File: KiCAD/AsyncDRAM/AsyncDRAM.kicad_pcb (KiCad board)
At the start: 2 copper layers, 13 parts, among them J1 UART, J2 SPI, J3 UPDI, J4 POWER

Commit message: Adjusted Design Rules, added MT6205 BGA footprint for fun
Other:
- net class Default: clearance 0.2 -> 0.2032; trace_width 0.25 -> 0.2032; via_dia 0.8 -> 0.9
- rule trace_clearance: 0.2 -> 0.2032
- rule trace_min: 0.2 -> 0.089
- rule via_min_drill: 0.3 -> 0.2
- rule via_min_size: 0.4 -> 0.45
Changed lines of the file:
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@@
   )
   (setup
-    (last_trace_width 0.25)
-    (trace_clearance 0.2)
+    (last_trace_width 0.2032)
+    (user_trace_width 0.089)
+    (trace_clearance 0.2032)
     (zone_clearance 0.508)
     (zone_45_only no)
-    (trace_min 0.2)
-    (via_size 0.8)
+    (trace_min 0.089)
+    (via_size 0.9)
     (via_drill 0.4)
-    (via_min_size 0.4)
-    (via_min_drill 0.3)
+    (via_min_size 0.45)
+    (via_min_drill 0.2)
+    (user_via 0.45 0.2)
     (uvia_size 0.3)
     (uvia_drill 0.1)
@@
   (net 40 MOSI)
   (net_class Default "This is the default net class."
-    (clearance 0.2)
-    (trace_width 0.25)
-    (via_dia 0.8)
+    (clearance 0.2032)
+    (trace_width 0.2032)
+    (via_dia 0.9)
     (via_drill 0.4)
     (uvia_dia 0.3)

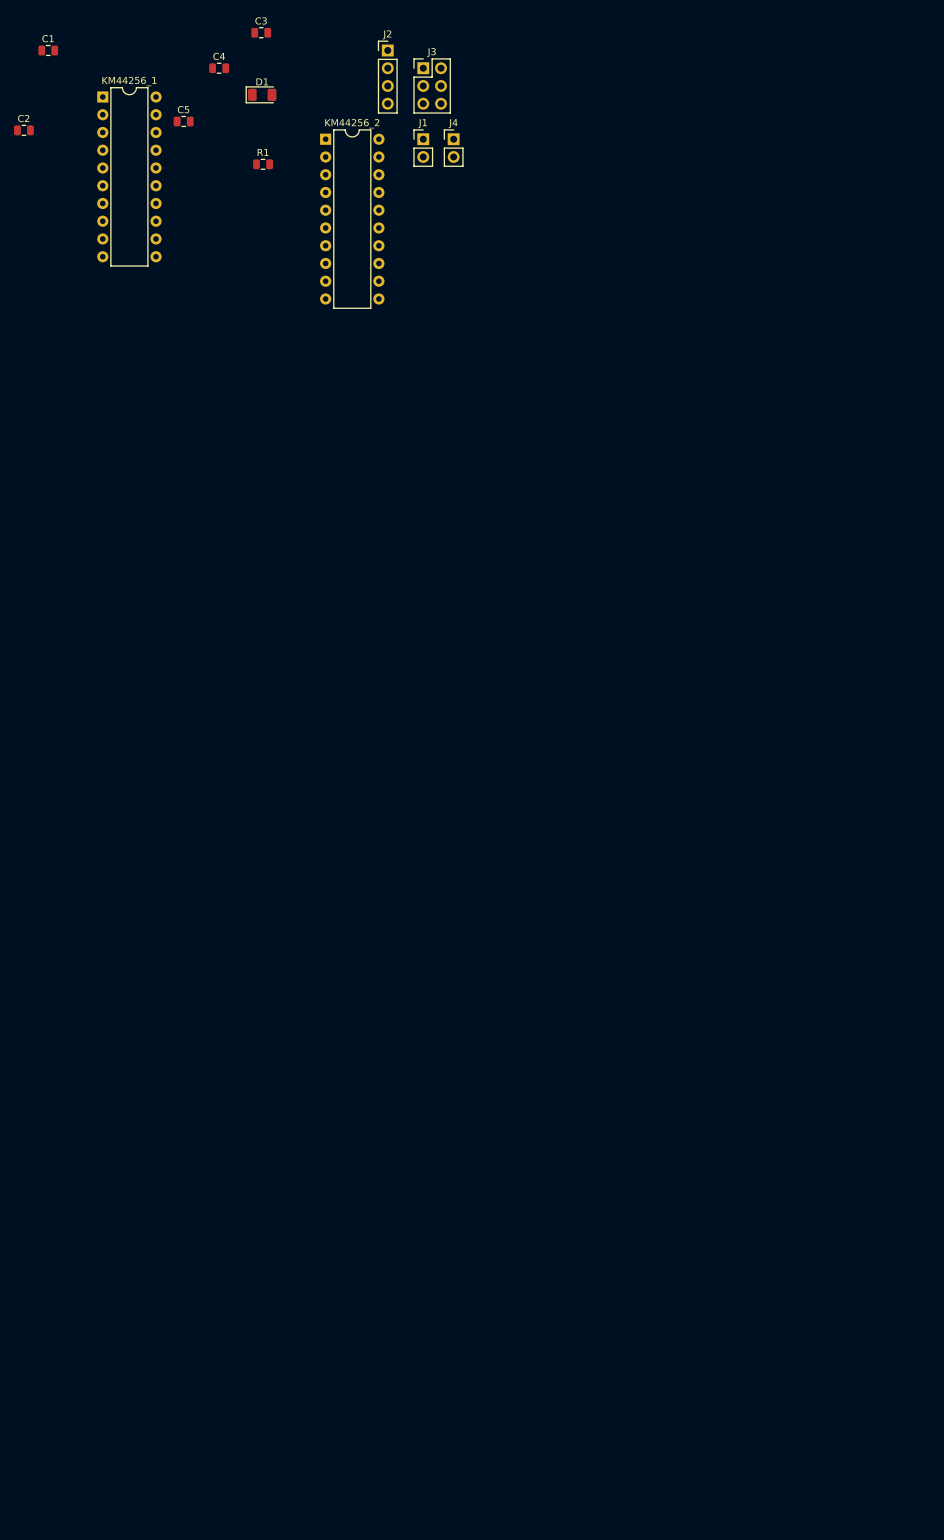
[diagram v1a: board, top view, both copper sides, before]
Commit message: Finalizing schematic, adding TQFP footprint, PCB outline
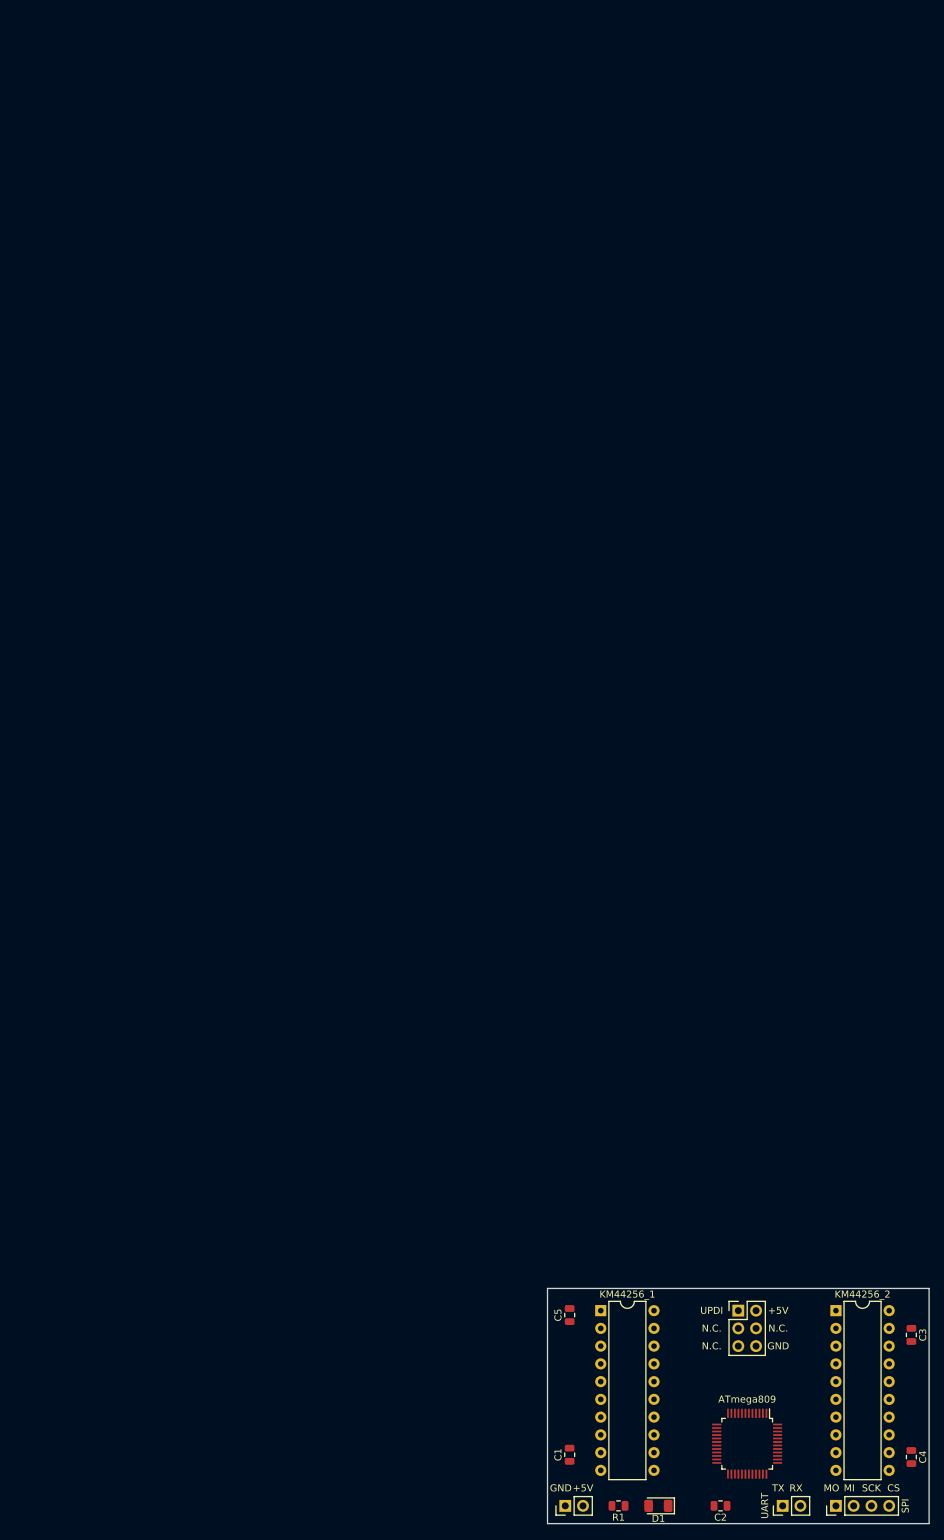
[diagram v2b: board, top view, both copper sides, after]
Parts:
- added ATmega809: ATmega809, QFP:TQFP-48_7x7mm_P0.5mm, F.Cu at (43.8, 184.2)
- moved C4 222.1 mm to (67.3, 186.1), turned to 270 degrees
- moved C2 220.7 mm to (40.0, 193.0), turned to 180 degrees
- moved J2 217.9 mm to (56.5, 193.0), turned to 90 degrees
- moved C1 214.4 mm to (18.4, 185.7), turned to 90 degrees
- moved D1 209.7 mm to (31.1, 193.0), turned to 180 degrees
- moved C3 208.3 mm to (67.3, 168.6), turned to 270 degrees
- moved J1 202.2 mm to (48.9, 193.0), turned to 90 degrees
- moved R1 198.6 mm to (25.4, 193.0), turned to 180 degrees
- moved J4 196.2 mm to (17.8, 193.0), turned to 90 degrees
- moved KM44256_1 187.7 mm to (22.9, 165.1)
- moved J3 183.4 mm to (42.5, 165.1)
- moved KM44256_2 182.9 mm to (56.5, 165.1)
- moved C5 179.5 mm to (18.4, 165.7), turned to 90 degrees
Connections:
- net Net-(ATM809_1-Pad1) renamed A0
- net Net-(ATM809_1-Pad2) renamed A1
- net Net-(ATM809_1-Pad3) renamed A2
- net Net-(ATM809_1-Pad4) renamed A3
- net Net-(ATM809_1-Pad5) renamed A4
- net Net-(ATM809_1-Pad6) renamed A5
- net Net-(ATM809_1-Pad7) renamed A6
- net Net-(ATM809_1-Pad8) renamed A7
- net Net-(ATM809_1-Pad9) renamed A8
- KM44256_1 pad 16: Net-(KM44256_1-Pad16) -> ~OE
- KM44256_1 pad 17: Net-(KM44256_1-Pad17) -> ~CAS
- KM44256_1 pad 3: Net-(KM44256_1-Pad3) -> ~W
- KM44256_1 pad 4: Net-(KM44256_1-Pad4) -> ~RAS
- KM44256_2 pad 16: Net-(KM44256_2-Pad16) -> ~OE
- KM44256_2 pad 17: Net-(KM44256_2-Pad17) -> ~CAS
- KM44256_2 pad 3: Net-(KM44256_2-Pad3) -> ~W
- KM44256_2 pad 4: Net-(KM44256_2-Pad4) -> ~RAS
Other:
- board outline added: 54.6 x 33.7 mm
- board text added: "+5V"
- board text added: "CS"
- board text added: "GND"
- board text added: "MI"
- board text added: "MO"
- board text added: "N.C."
- board text added: "RX"
- board text added: "SCK"
- board text added: "TX"
- board text added: "UPDI"

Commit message: GND Planes
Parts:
- turned ATmega809 to 0 degrees
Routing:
- added copper zone on B.Cu, net GND
- added copper zone on F.Cu, net GND
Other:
- net class Default: clearance 0.2032 -> 0.127
- rule trace_clearance: 0.2032 -> 0.127
- board text removed: "N.C."

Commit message: Adjusted board settings to Elecrow Specifications
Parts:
- renumbered ATmega809 to ATM809_1
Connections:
- net Net-(ATM809_1-Pad41) renamed UPDI
- D1 pad 1: GND -> Net-(D1-Pad1)
- D1 pad 2: Net-(D1-Pad2) -> +5V
- R1 pad 1: Net-(D1-Pad2) -> GND
- R1 pad 2: +5V -> Net-(D1-Pad1)
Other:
- net class Default: clearance 0.127 -> 0.1524; trace_width 0.2032 -> 0.1524; via_dia 0.9 -> 0.6048; via_drill 0.4 -> 0.3
- rule trace_clearance: 0.127 -> 0.1524
- rule trace_min: 0.089 -> 0.1524
- rule via_min_drill: 0.2 -> 0.3
- rule via_min_size: 0.45 -> 0.6048

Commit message: Started PCB Routing...
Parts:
- turned ATM809_1 to 90 degrees
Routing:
- net +5V: track 0.00 -> 83.4 mm
- net A0: track 0.00 -> 53.9 mm, vias 0 -> 1
- net A3: track 0.00 -> 53.2 mm, vias 0 -> 3
- net A7: track 0.00 -> 51.6 mm, vias 0 -> 2
- net A6: track 0.00 -> 48.9 mm, vias 0 -> 2
- net A4: track 0.00 -> 45.5 mm
- net A5: track 0.00 -> 45.3 mm, vias 0 -> 2
- net A1: track 0.00 -> 33.6 mm, vias 0 -> 1
- net A2: track 0.00 -> 32.0 mm
- net Net-(D1-Pad1): track 0.00 -> 9.53 mm
- net A8: track 0.00 -> 2.74 mm

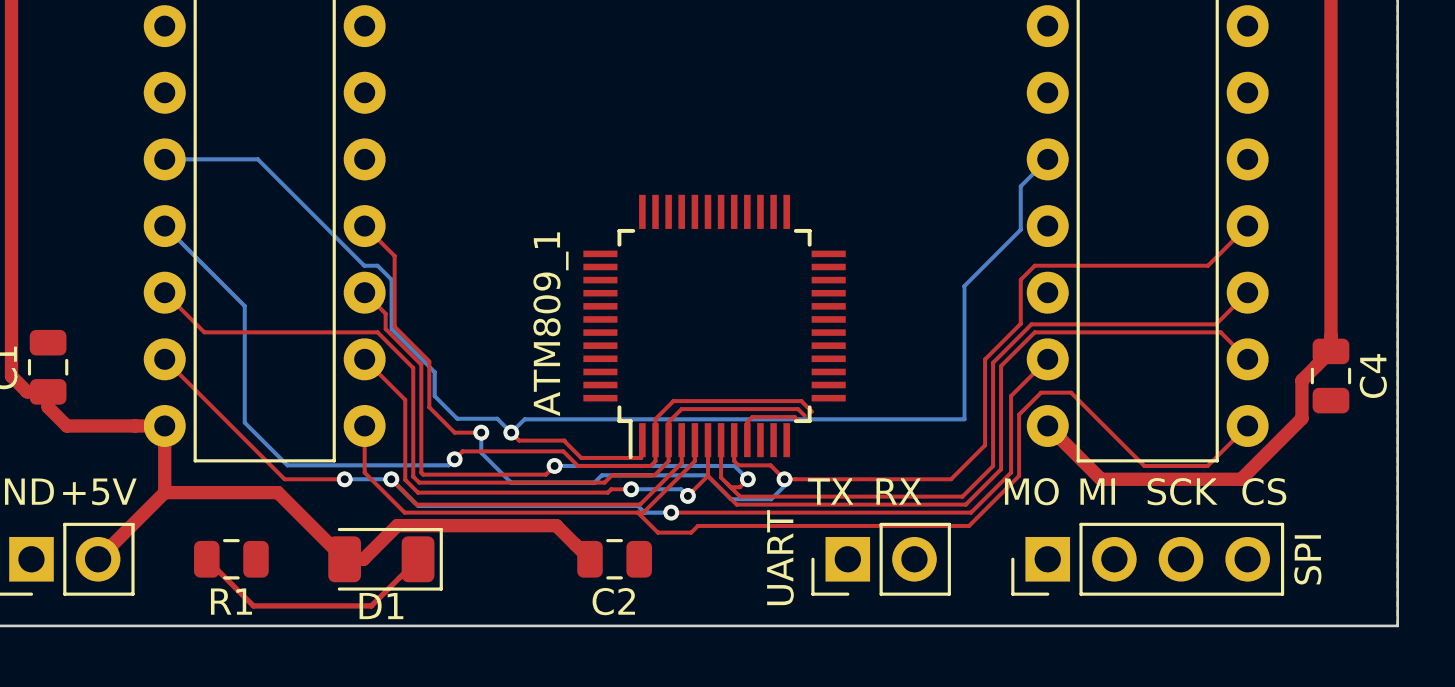
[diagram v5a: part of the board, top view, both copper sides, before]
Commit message: PCB Routing Update
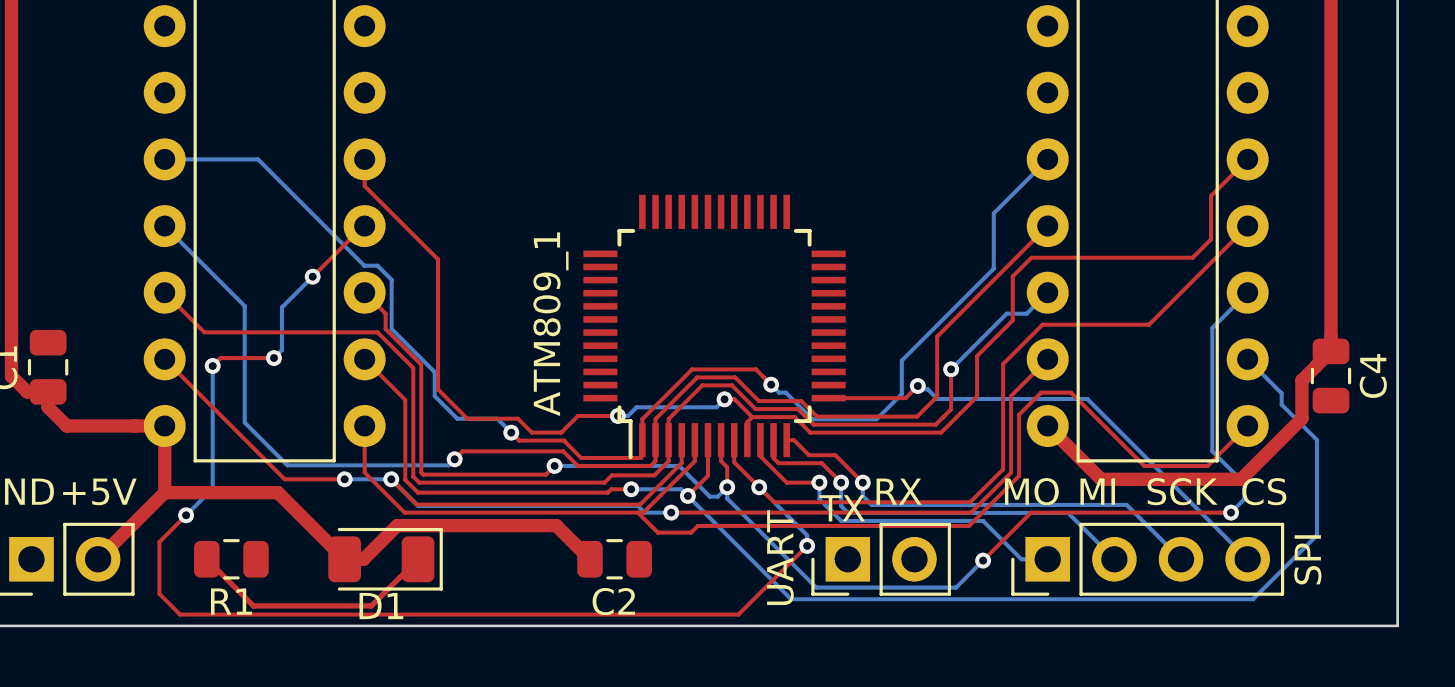
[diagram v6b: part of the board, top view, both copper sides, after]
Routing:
- net A8: track 2.74 -> 50.6 mm, vias 0 -> 2
- net A7: track 51.6 -> 75.3 mm, vias 2 -> 6
- net SS: track 0.00 -> 18.9 mm, vias 0 -> 1
- net SCK: track 0.00 -> 17.2 mm, vias 0 -> 1
- net MISO: track 0.00 -> 15.8 mm, vias 0 -> 1
- net A1: track 33.6 -> 47.8 mm
- net MOSI: track 0.00 -> 13.6 mm, vias 0 -> 1
- net A2: track 32.0 -> 45.2 mm, vias 0 -> 1
- net A5: track 45.3 -> 53.2 mm
- net A6: track 48.9 -> 54.0 mm, vias 2 -> 4
- net A0: track 53.9 -> 49.1 mm, vias 1 -> 2

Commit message: PCB Routing Bottom Half done
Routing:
- net RxD: track 0.00 -> 61.2 mm, vias 0 -> 5
- net TxD: track 0.00 -> 53.0 mm, vias 0 -> 6
- net +5V: track 83.4 -> 123.0 mm, vias 0 -> 3
- net A3: track 53.2 -> 55.5 mm
- net A0: track 49.1 -> 46.9 mm
- net GND: track 0.00 -> 0.97 mm
- net Net-(D1-Pad1): track 9.53 -> 8.97 mm

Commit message: Fixed LED finally
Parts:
- turned C2 to 270 degrees
- turned R1 to 270 degrees
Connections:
- D1 pad 1: Net-(D1-Pad1) -> GND
- D1 pad 2: +5V -> Net-(D1-Pad2)
- R1 pad 1: GND -> Net-(D1-Pad2)
- R1 pad 2: Net-(D1-Pad1) -> +5V
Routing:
- net Net-(D1-Pad1): track 8.97 -> 0.00 mm
- net Net-(D1-Pad2): track 0.00 -> 4.70 mm
- net +5V: track 123.0 -> 121.6 mm, vias 3 -> 5
- net GND: track 0.97 -> 0.00 mm
